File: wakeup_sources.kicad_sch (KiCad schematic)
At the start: 9 parts, among them SW1 SW_Push, U1 MCP7940N-xMNY, U5 DRV5032FC, Y1 32.768kHz

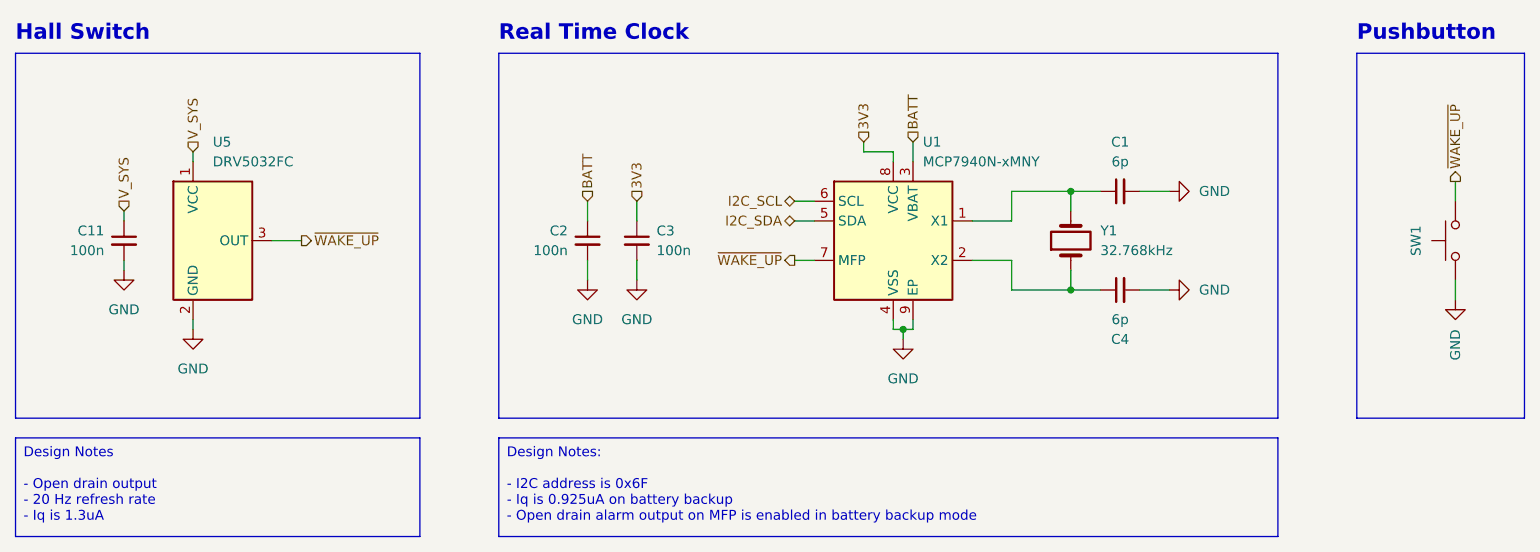
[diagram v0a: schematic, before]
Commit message: update to kicad 9.0
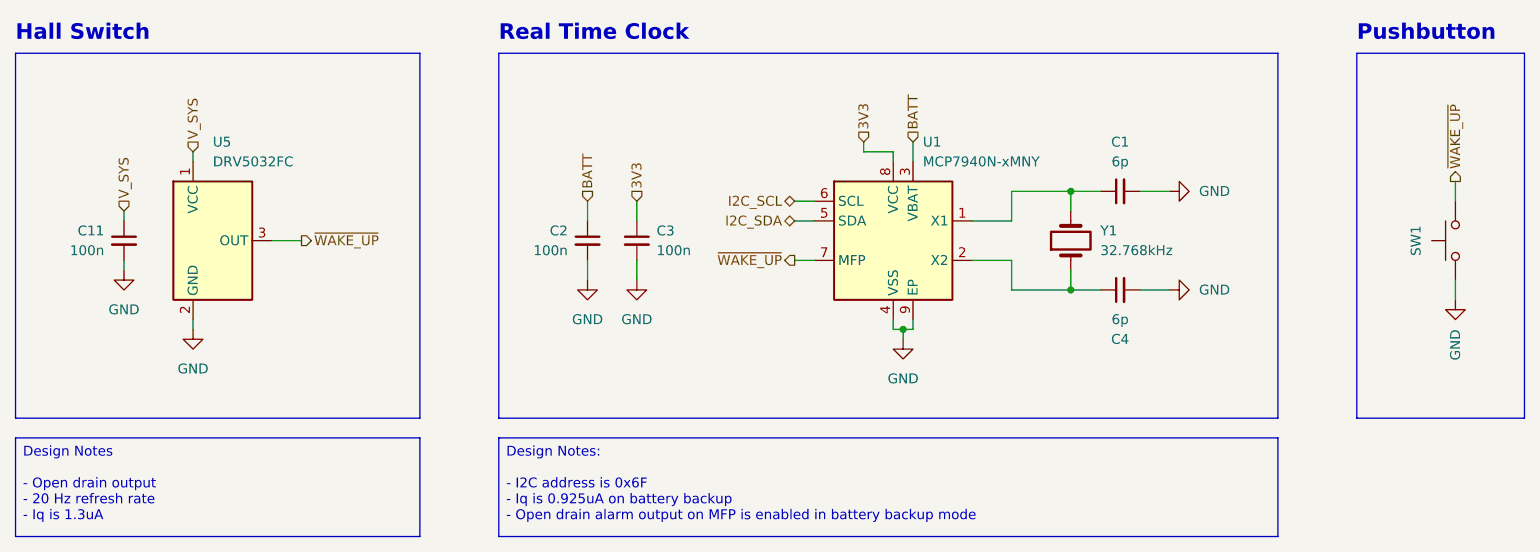
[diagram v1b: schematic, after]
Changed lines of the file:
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@@
 (kicad_sch
-	(version 20231120)
+	(version 20250114)
 	(generator "eeschema")
-	(generator_version "8.0")
+	(generator_version "9.0")
 	(paper "A4")
 	(title_block
@@
 		(comment 4 "Open-drain wakeup sources")
 	)
+	(rectangle
+		(start 220.98 59.69)
+		(end 242.57 106.68)
+		(stroke
+			(width 0)
+			(type default)
+		)
+		(fill
+			(type none)
+		)
+	)
+	(rectangle
+		(start 110.49 59.69)
+		(end 210.82 106.68)
+		(stroke
+			(width 0)
+			(type default)
+		)
+		(fill
+			(type none)
+		)
+	)
+	(rectangle
+		(start 48.26 59.69)
+		(end 100.33 106.68)
+		(stroke
+			(width 0)
+			(type default)
+		)
+		(fill
+			(type none)
+		)
+	)
+	(text "Hall Switch"
+		(exclude_from_sim no)
+		(at 48.26 57.15 0)
+		(effects
+			(font
+				(size 2 2)
+				(thickness 0.4)
+				(bold yes)
+			)
+			(justify left)
+		)
+	)
+	(text "Pushbutton"
+		(exclude_from_sim no)
+		(at 220.98 57.15 0)
+		(effects
+			(font
+				(size 2 2)
+				(thickness 0.4)
+				(bold yes)
+			)
+			(justify left)
+		)
+	)
+	(text "Real Time Clock"
+		(exclude_from_sim no)
+		(at 110.49 57.15 0)
+		(effects
+			(font
+				(size 2 2)
+				(thickness 0.4)
+				(bold yes)
+			)
+			(justify left)
+		)
+	)
+	(text_box "Design Notes\n\n- Open drain output\n- 20 Hz refresh rate\n- Iq is 1.3uA"
+		(exclude_from_sim no)
+		(at 48.26 109.22 0)
+		(size 52.07 12.7)
+		(margins 0.9525 0.9525 0.9525 0.9525)
+		(stroke
+			(width 0)
+			(type default)
+		)
+		(fill
+			(type color)
+			(color 255 255 194 1)
+		)
+		(effects
+			(font
+				(size 1.27 1.27)
+			)
+			(justify left top)
+		)
+	)
+	(text_box "Design Notes:\n\n- I2C address is 0x6F\n- Iq is 0.925uA on battery backup\n- Open drain alarm output on MFP is enabled in battery backup mode"
+		(exclude_from_sim no)
+		(at 110.49 109.22 0)
+		(size 100.33 12.7)
+		(margins 0.9525 0.9525 0.9525 0.9525)
+		(stroke
+			(width 0)
+			(type default)
+		)
+		(fill
+			(type color)
+			(color 255 255 194 1)
+		)
+		(effects
+			(font
+				(size 1.27 1.27)
+				(thickness 0.1588)
+			)
+			(justify left top)
+		)
+	)
 	(junction
 		(at 162.56 95.25)
@@
 		)
 	)
-	(rectangle
-		(start 220.98 59.69)
-		(end 242.57 106.68)
-		(stroke
-			(width 0)
-			(type default)
-		)
-		(fill
-			(type none)
-		)
-	)
-	(rectangle
-		(start 110.49 59.69)
-		(end 210.82 106.68)
-		(stroke
-			(width 0)
-			(type default)
-		)
-		(fill
-			(type none)
-		)
-	)
-	(rectangle
-		(start 48.26 59.69)
-		(end 100.33 106.68)
-		(stroke
-			(width 0)
-			(type default)
-		)
-		(fill
-			(type none)
-		)
-	)
-	(text_box "Design Notes\n\n- Open drain output\n- 20 Hz refresh rate\n- Iq is 1.3uA"
-		(exclude_from_sim no)
-		(at 48.26 109.22 0)
-		(size 52.07 12.7)
-		(stroke
-			(width 0)
-			(type default)
-		)
-		(fill
-			(type color)
-			(color 255 255 194 1)
-		)
-		(effects
-			(font
-				(size 1.27 1.27)
-			)
-			(justify left top)
-		)
-	)
-	(text_box "Design Notes:\n\n- I2C address is 0x6F\n- Iq is 0.925uA on battery backup\n- Open drain alarm output on MFP is enabled in battery backup mode"
-		(exclude_from_sim no)
-		(at 110.49 109.22 0)
-		(size 100.33 12.7)
-		(stroke
-			(width 0)
-			(type default)
-		)
-		(fill
-			(type color)
-			(color 255 255 194 1)
-		)
-		(effects
-			(font
-				(size 1.27 1.27)
-				(thickness 0.1588)
-			)
-			(justify left top)
-		)
-	)
-	(text "Hall Switch"
-		(exclude_from_sim no)
-		(at 48.26 57.15 0)
-		(effects
-			(font
-				(size 2 2)
-				(thickness 0.4)
-				(bold yes)
-			)
-			(justify left)
-		)
-	)
-	(text "Pushbutton"
-		(exclude_from_sim no)
-		(at 220.98 57.15 0)
-		(effects
-			(font
-				(size 2 2)
-				(thickness 0.4)
-				(bold yes)
-			)
-			(justify left)
-		)
-	)
-	(text "Real Time Clock"
-		(exclude_from_sim no)
-		(at 110.49 57.15 0)
-		(effects
-			(font
-				(size 2 2)
-				(thickness 0.4)
-				(bold yes)
-			)
-			(justify left)
-		)
-	)
 	(hierarchical_label "3V3"
 		(shape input)
 		(at 128.27 78.74 90)
-		(fields_autoplaced yes)
 		(effects
 			(font
@@
 		(shape input)
 		(at 121.92 78.74 90)
-		(fields_autoplaced yes)
 		(effects
 			(font
@@
 		(shape bidirectional)
 		(at 148.59 78.74 180)
-		(fields_autoplaced yes)
 		(effects
 			(font
@@
 		(shape input)
 		(at 62.23 80.01 90)
-		(fields_autoplaced yes)
 		(effects
 			(font
@@
 		(shape input)
 		(at 163.83 71.12 90)
-		(fields_autoplaced yes)
 		(effects
 			(font
@@
 		(shape output)
 		(at 233.68 76.2 90)
-		(fields_autoplaced yes)
 		(effects
 			(font
@@
 		(shape input)
 		(at 157.48 71.12 90)
-		(fields_autoplaced yes)
 		(effects
 			(font
@@
 		(shape input)
 		(at 71.12 72.39 90)
-		(fields_autoplaced yes)
 		(effects
 			(font
@@
 		(shape bidirectional)
 		(at 148.59 81.28 180)
-		(fields_autoplaced yes)
 		(effects
 			(font
@@
 		(shape output)
 		(at 148.59 86.36 180)
-		(fields_autoplaced yes)
 		(effects
 			(font
@@
 		(shape output)
 		(at 85.09 83.82 0)
-		(fields_autoplaced yes)
-		(effects
-			(font
+		(effects
+			(font
